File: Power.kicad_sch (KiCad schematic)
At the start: 29 parts, among them Q1 SIS412DN-T1-GE3, Q2 SIS412DN-T1-GE3, Q9 BSS84, U11 MCP1703Ax-330xxDB, U12 LTC4365TS8

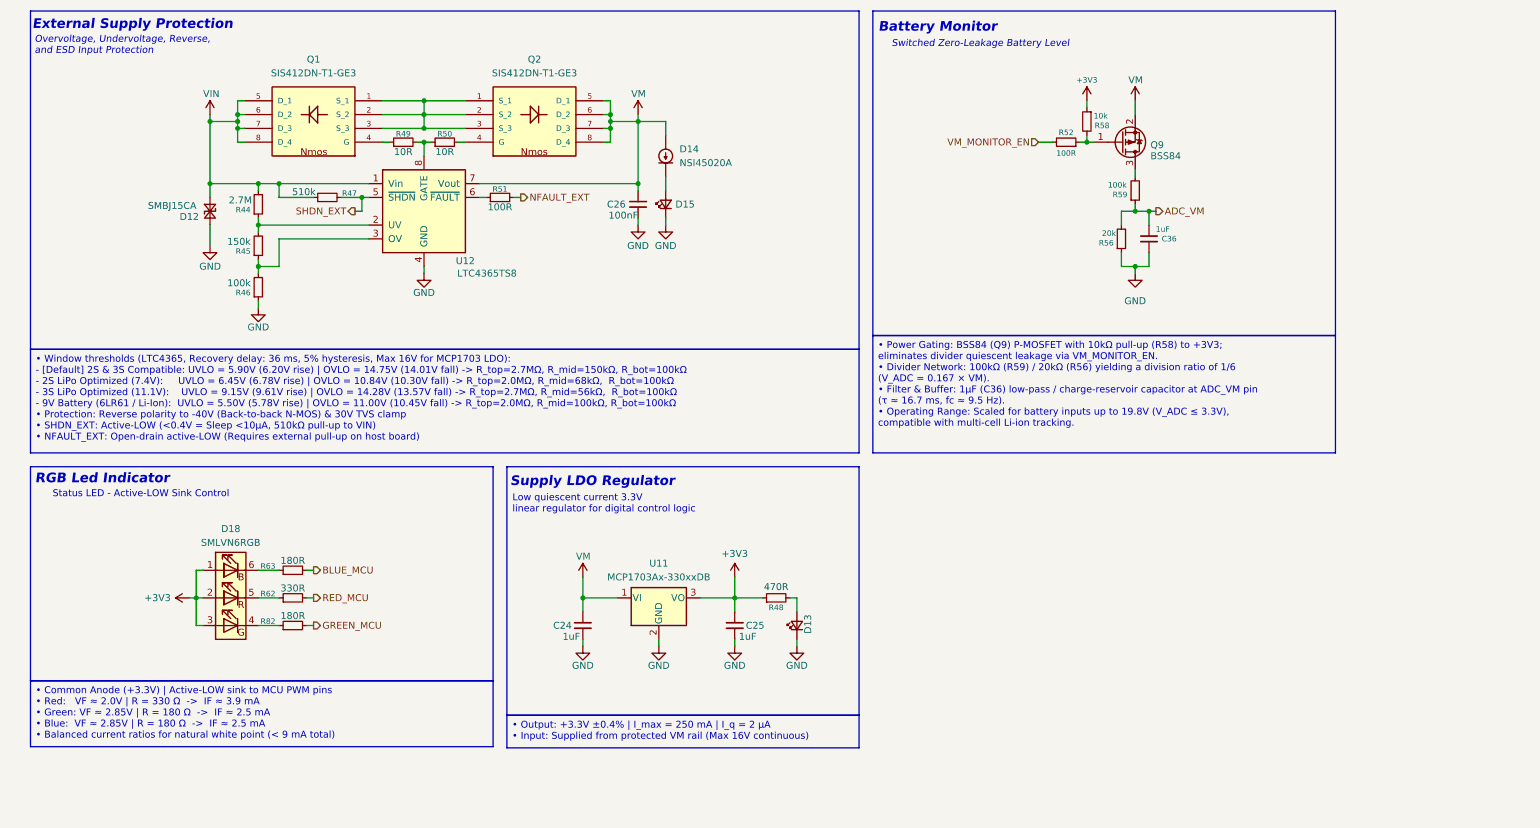
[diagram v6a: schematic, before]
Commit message: feat: switch to JST-GH connectors and add TPD4E05U06 TVS protection for SPI/I2C
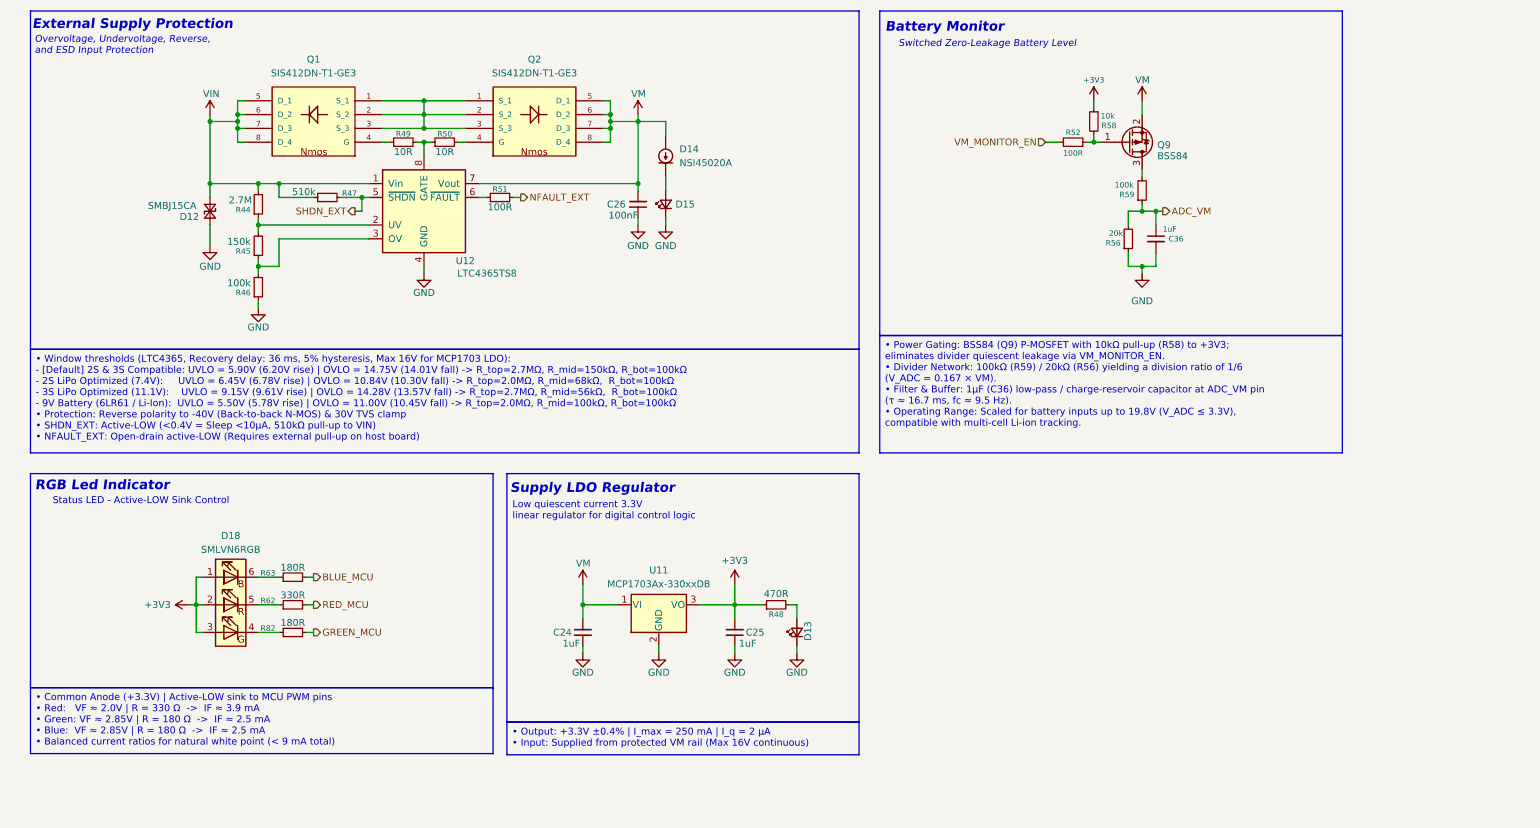
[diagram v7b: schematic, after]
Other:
- moved on the sheet: C24, C25, C36, D13, D18, Q9, R48, R52, R56, R58, R59, R62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

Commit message: feat: finalize STM32G070CBT6 LQFP48 pinout and peripheral mapping
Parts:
- removed R52: 100R, Resistor_SMD:R_0603_1608Metric, symbol Device:R_Small
- added Q3: BSS138, Package_TO_SOT_SMD:SOT-23, symbol Transistor_FET:BSS138
- added R87: 100R, Resistor_SMD:R_0603_1608Metric, symbol Device:R_Small
- added R94: 10k, Resistor_SMD:R_0603_1608Metric, symbol Device:R_Small
- C36: value 1uF -> 10nF
- D12: value SMBJ15CA -> SMBJ30CA
- R51: value 100R -> 22R
- R58: value 10k -> 100k
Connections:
- net +3V3: no longer R58.1
- net GND: now also Q3.2 (S), R94.2
- net VM: now also R58.1
- net VM_MONITOR_EN: now also R87.1
- net at Q9.1 (G), R58.2: now also Q3.3 (D)
- new net: Q3.1 (G), R87.2, R94.1
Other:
- note added: "Switched Battery Monitor"
- note removed: "Battery Monitor"
- moved on the sheet: C36, Q9, R56, R58, R59
